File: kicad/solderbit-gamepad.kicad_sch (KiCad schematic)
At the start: 39 parts, among them SW1 DPDT, U1 Shift_Register_74HC165D

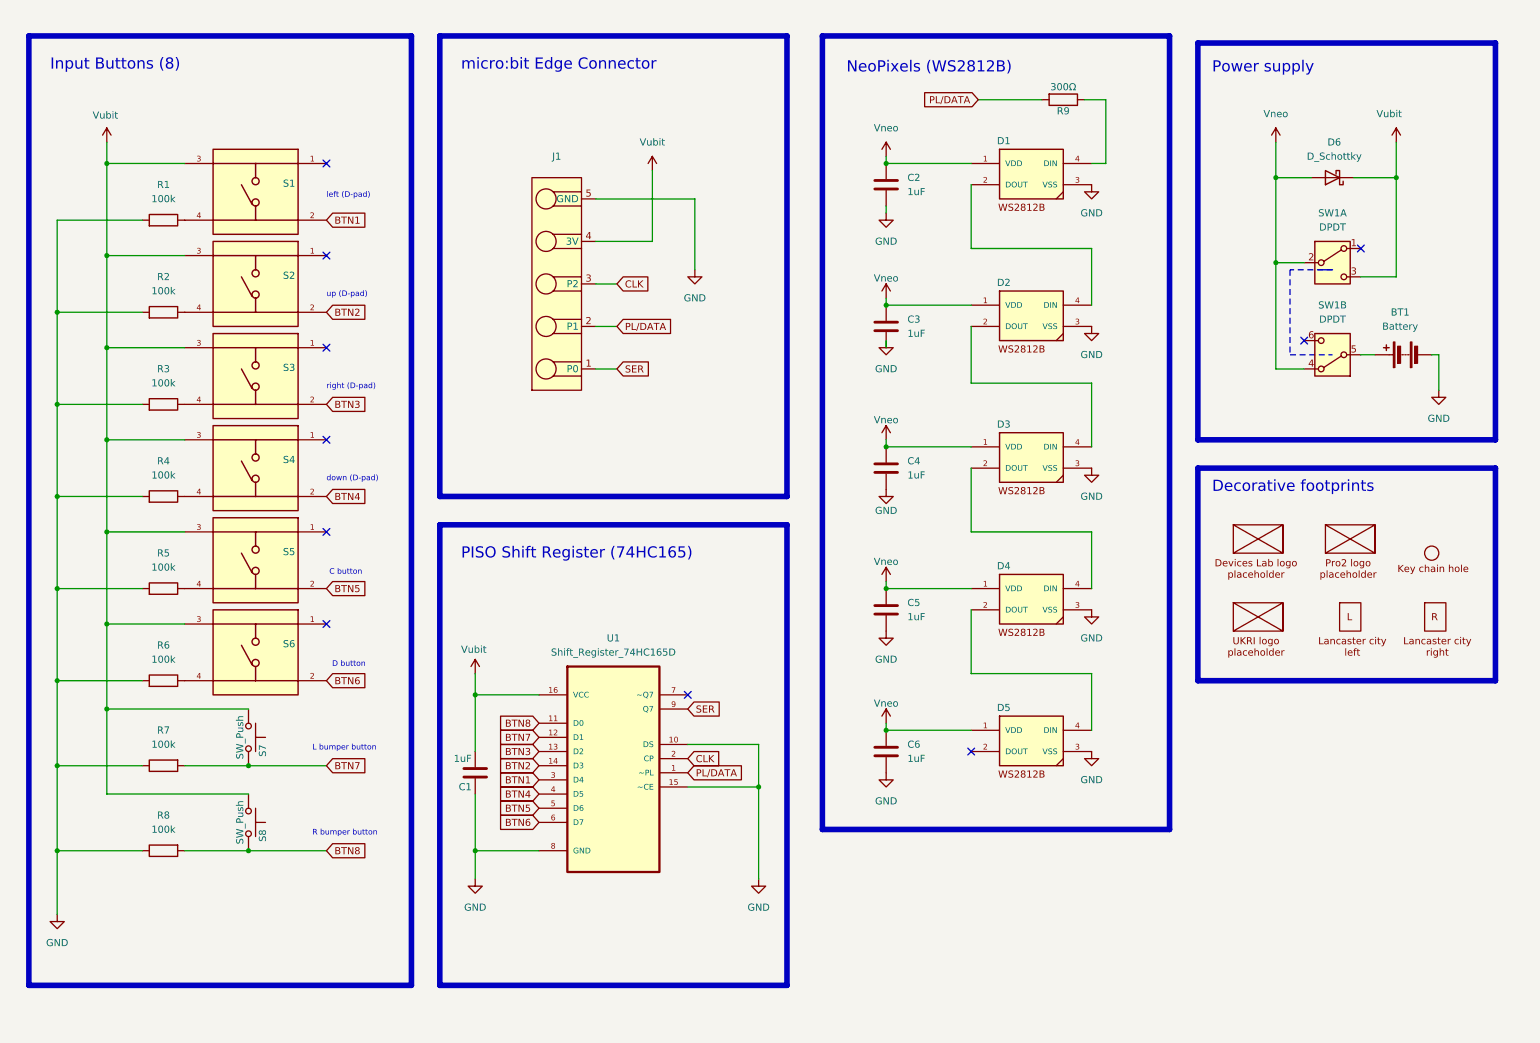
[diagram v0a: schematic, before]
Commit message: KiCad font fixes and 3D renders
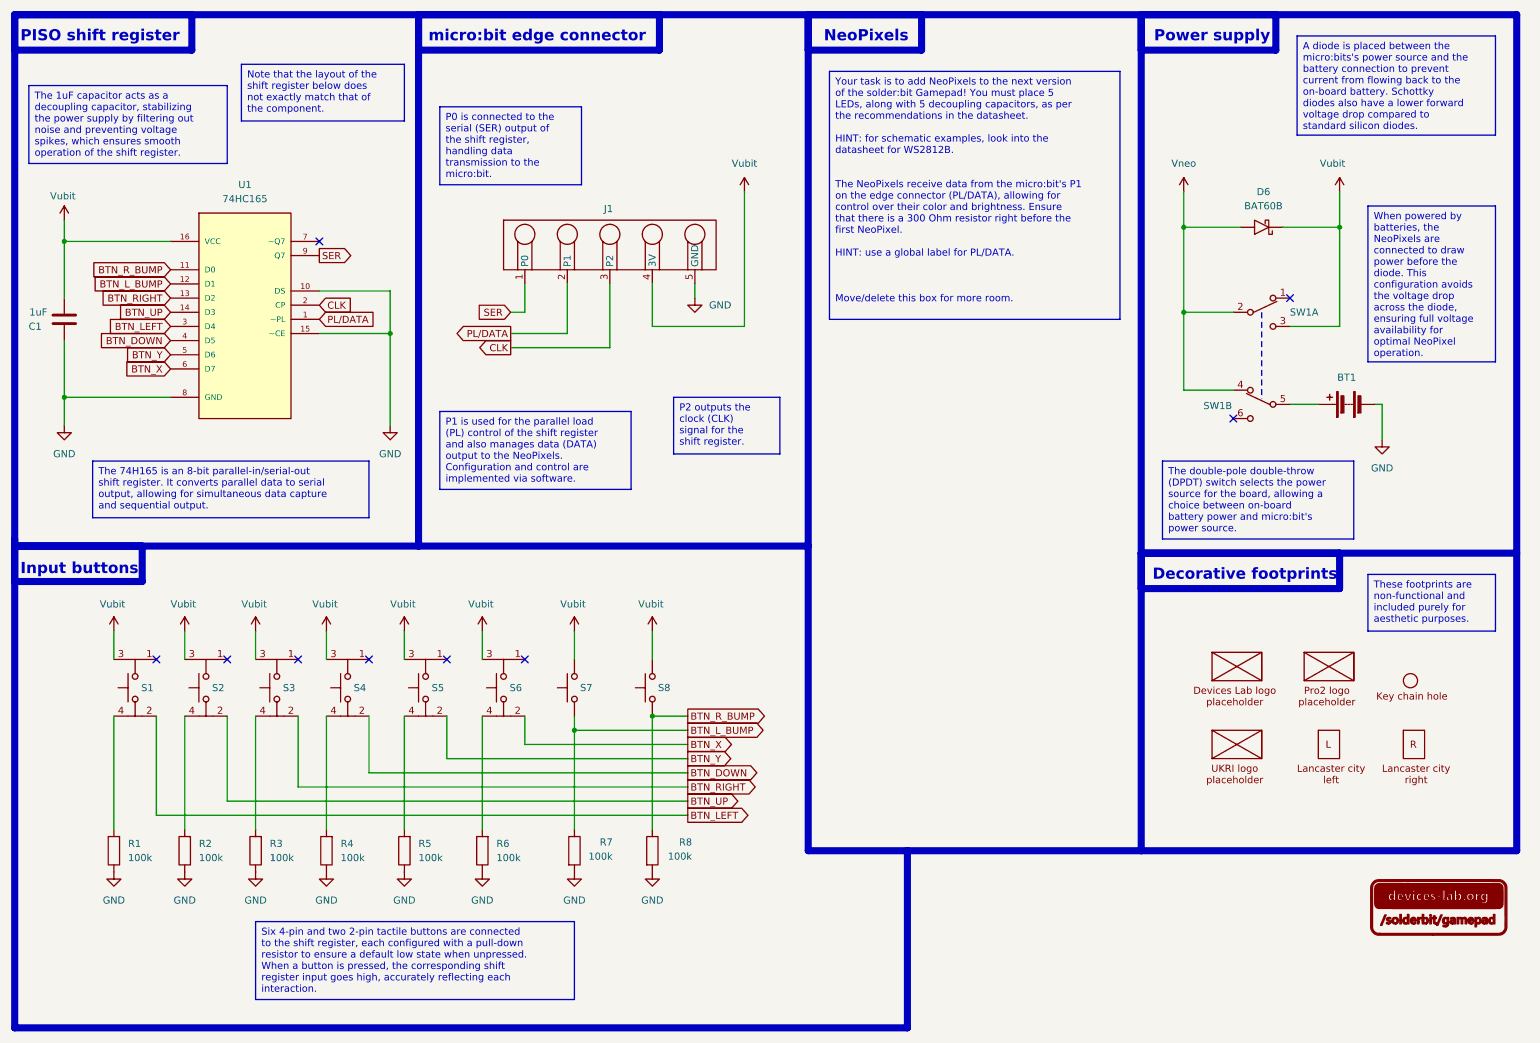
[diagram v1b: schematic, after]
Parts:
- removed C2, C3, C4, C5, C6: 1uF, Solderbit_Gamepad:1206_Capacitor, symbol Device:C
- removed D1, D2, D3, D4, D5: NeoPixel_WS2812B, Solderbit_Gamepad:NeoPixel_WS2812B, symbol Solderbit_Gamepad:NeoPixel_WS2812B
- removed R1, R2, R3, R4, R5, R6, R7, R8: 100k, Solderbit_Gamepad:1206_Resistor, symbol Device:R
- removed R9: 300Ω, Solderbit_Gamepad:1206_Resistor, symbol Device:R
- removed S1: ~, Solderbit_Gamepad:Tactile_Switch, symbol Solderbit_Gamepad:Tactile_Switch_Button
- removed S8: SW_Push, Solderbit_Gamepad:Tactile_Switch_Right_90_Degrees, symbol Switch:SW_Push
- added R1, R2, R3, R4, R5, R6, R7, R8: 100k, Solderbit_Gamepad:1206_Resistor, symbol Solderbit_Gamepad:Resistor
- added S1: TS-1002S-AR06026, Solderbit_Gamepad:Tactile_Switch, symbol Solderbit_Gamepad:Tactile_Switch_4_Pin
- added S8: TS-1037-A4B3-D2, Solderbit_Gamepad:Tactile_Switch_Right_90_Degrees, symbol Solderbit_Gamepad:Tactile_Switch_2_Pin
- BT1: value Battery -> BH-AAA-B5AA001
- C1: symbol Device:C -> Solderbit_Gamepad:Capacitor
- D6: value D_Schottky -> BAT60B; symbol Device:D_Schottky -> Solderbit_Gamepad:Schottky_Diode
- J1: value ~ -> Microbit; now left out of the parts list
- S2, S3, S4, S5, S6: value ~ -> TS-1002S-AR06026; symbol Solderbit_Gamepad:Tactile_Switch_Button -> Solderbit_Gamepad:Tactile_Switch_4_Pin
- S7: value SW_Push -> TS-1037-A4B3-D2; symbol Switch:SW_Push -> Solderbit_Gamepad:Tactile_Switch_2_Pin
- SW1: value DPDT -> MST22D18G2 125; symbol Switch:SW_DPDT_x2 -> Solderbit_Gamepad:Sliding_Switch_DPDT
- U1: value Shift_Register_74HC165D -> 74HC165
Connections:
- net GND: now also R1.2, R2.2, R3.2, R4.2, R5.2, R6.2, R7.1, R8.1
- net Vubit: now also S1.3, S8.1
- net at S2.4: now also R2.1
- net at S4.4: now also R4.1
- net at S6.4: now also R6.1
- net at S5.4: now also R5.1
- net at S3.4: now also R3.1
- net BTN1 renamed BTN_LEFT
- net BTN_LEFT: now also S1.2
- net BTN2 renamed BTN_UP
- net BTN3 renamed BTN_RIGHT
- net BTN4 renamed BTN_DOWN
- net BTN5 renamed BTN_Y
- net BTN6 renamed BTN_X
- net BTN7 renamed BTN_L_BUMP
- net BTN_L_BUMP: now also R7.2
- net BTN8 renamed BTN_R_BUMP
- net BTN_R_BUMP: now also R8.2, S8.2
- new net: R1.1, S1.4
- no-connect marks 10 -> 9
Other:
- note added: "Input buttons"
- note added: "NeoPixels"
- note added: "PISO shift register"
- note added: "micro:bit edge connector"
- note removed: "C button"
- note removed: "D button"
- note removed: "Input Buttons (8)"
- note removed: "L bumper button"
- note removed: "NeoPixels (WS2812B)"
- note removed: "PISO Shift Register (74HC165)"
- note removed: "R bumper button"
- note removed: "down (D-pad)"
- note removed: "left (D-pad)"
- note removed: "micro:bit Edge Connector"
- note removed: "right (D-pad)"
- note removed: "up (D-pad)"
- company: Aron Eggens -> pro² network+
- moved on the sheet: BT1, C1, S7, U1
